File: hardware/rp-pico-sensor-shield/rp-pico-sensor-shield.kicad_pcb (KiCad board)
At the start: 2 copper layers, 87 x 65 mm, 43 parts, among them J1 Barrel_Jack, J10 Conn_01x04, J11 Conn_01x04, J12 Conn_01x04, J13 Conn_01x04, J14 Conn_01x04, J15 Conn_01x04, J16 Conn_01x04, J17 Conn_01x03, J18 Conn_01x03, J19 Conn_01x03, J2 Conn_01x04, J20 Conn_01x03, J21 Conn_01x03, J22 Conn_01x03, J23 Conn_01x04, J24 Screw Terminal, J25 Conn_01x04, J26 I2C0, J27 I2C1, J28 AGND, J29 Conn_01x03, J3 Conn_01x04, J4 Conn_01x04, J5 Conn_01x04, J6 Conn_01x04, J7 Conn_01x04, J8 Conn_01x04, J9 Conn_01x04, Q1 DMG2305UX, SW1 SW_Push, U1 NCP1117-5.0_SOT223, U2 Pico

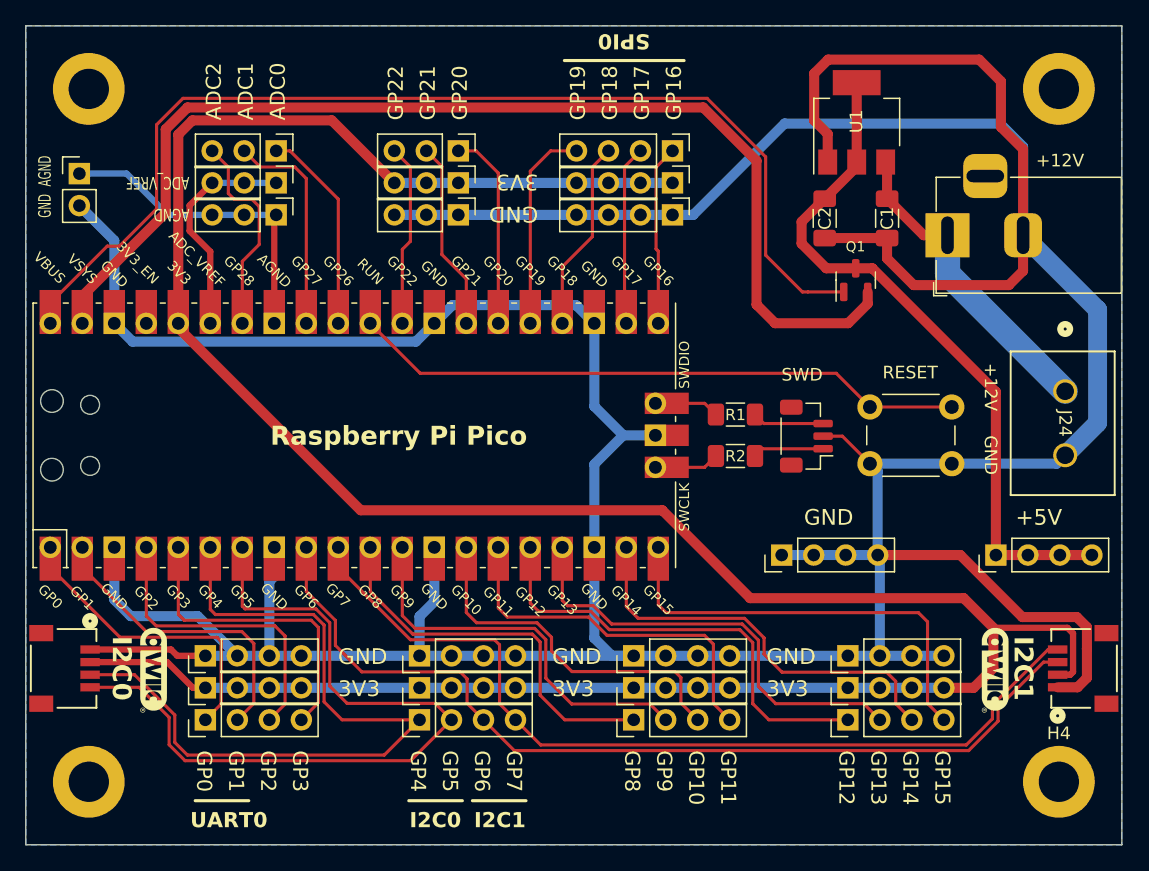
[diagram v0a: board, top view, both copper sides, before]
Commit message: serperated I2C busses for display and gyro
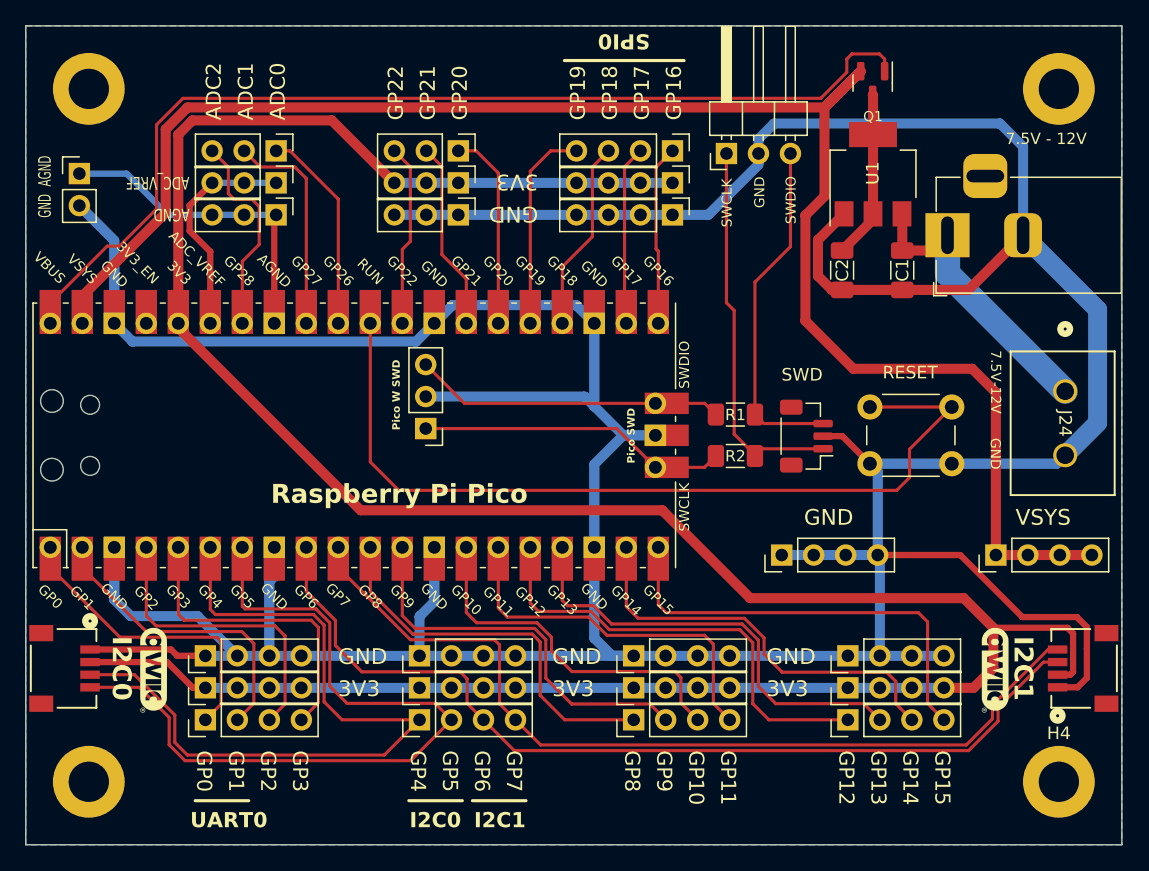
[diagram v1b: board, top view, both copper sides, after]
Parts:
- added J30: Conn_01x03, Connector_PinHeader_2.54mm:PinHeader_1x03_P2.54mm_Vertical, F.Cu at (81.7, 82.0)
- added J31: Conn_01x03, Connector_PinHeader_2.54mm:PinHeader_1x03_P2.54mm_Horizontal, F.Cu at (105.6, 60.1)
- moved Q1 15.7 mm to (117.2, 54.5), turned to -90 degrees
- moved C2 4.34 mm to (114.8, 69.4)
- moved U1 4.31 mm to (117.2, 61.8)
- moved C1 4.29 mm to (119.6, 69.4)
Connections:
- J25 pad 1: +5V -> VSYS
- J25 pad 2: +5V -> VSYS
- J25 pad 3: +5V -> VSYS
- J25 pad 4: +5V -> VSYS
- Q1 pad 2: Net-(Q1-S) -> VSYS
- U2 pad 39: Net-(Q1-S) -> VSYS
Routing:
- net VSYS: track 0.00 -> 134.8 mm
- net Net-(Q1-S): track 89.9 -> 0.00 mm
- net +5V: track 55.5 -> 13.4 mm
- net Net-(J29-Pin_1): track 5.65 -> 30.6 mm
- net Net-(J29-Pin_3): track 5.70 -> 27.6 mm
- net RESET: track 48.9 -> 68.6 mm
- net SWDIO: track 5.17 -> 24.7 mm
- net SWCLK: track 5.17 -> 24.7 mm
- net GND: track 395.4 -> 376.3 mm
- net Net-(Q1-G): track 86.2 -> 81.7 mm
- net +12V: track 25.2 -> 23.3 mm
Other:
- board text added: "7.5V - 12V"
- board text added: "7.5V-12V"
- board text added: "Pico SWD"
- board text added: "Pico W SWD"
- board text added: "SWCLK"
- board text added: "SWDIO"
- board text added: "VSYS"
- board text added: "v1.3"
- board text removed: "+12V"
- board text removed: "+5V"
- board text removed: "v1.2"
